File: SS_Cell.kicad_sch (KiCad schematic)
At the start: 12 parts, among them J1 SSC1, U1 ATtiny102-SS, U2 TPS2115

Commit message: 
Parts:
- removed R1, R2, R24: 5K, Resistor_SMD:R_0603_1608Metric, symbol Device:R
- removed TP1: SSC_TPIDATA, TestPoint:TestPoint_Pad_D1.0mm, symbol Connector:TestPoint
- removed TP2: SSC_TPICLK, TestPoint:TestPoint_Pad_D1.0mm, symbol Connector:TestPoint
- removed TP3: SSC_RST, TestPoint:TestPoint_Pad_D1.0mm, symbol Connector:TestPoint
- removed U1: ATtiny102-SS, Package_SO:SOIC-8_3.9x4.9mm_P1.27mm, symbol MCU_Microchip_ATtiny:ATtiny102-SS
- C9: renamed from C1; MPN (none) -> C14663
- J1: now left out of the parts list
- R24: renamed from R25; footprint Resistor_SMD:R_0603_1608Metric -> Resistor_SMD:R_0402_1005Metric; symbol Device:R -> Project:R; MPN (none) -> C477765
- R25: renamed from R26; footprint Resistor_SMD:R_0603_1608Metric -> Resistor_SMD:R_0402_1005Metric; symbol Device:R -> Project:R; MPN (none) -> C25130
- U4: renamed from U2; footprint Package_SO:TSSOP-8_4.4x3mm_P0.65mm -> Library:VSON-8_3.3x3.3mm_P0.65mm_NexFET; JLCPCB Rotation Offset (none) -> -90; MPN (none) -> C140321
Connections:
- net SS_TX: now reaches J1.2 (Pin_2)
- net SS_RX: now reaches J1.3 (Pin_3)
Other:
- moved on the sheet: J1

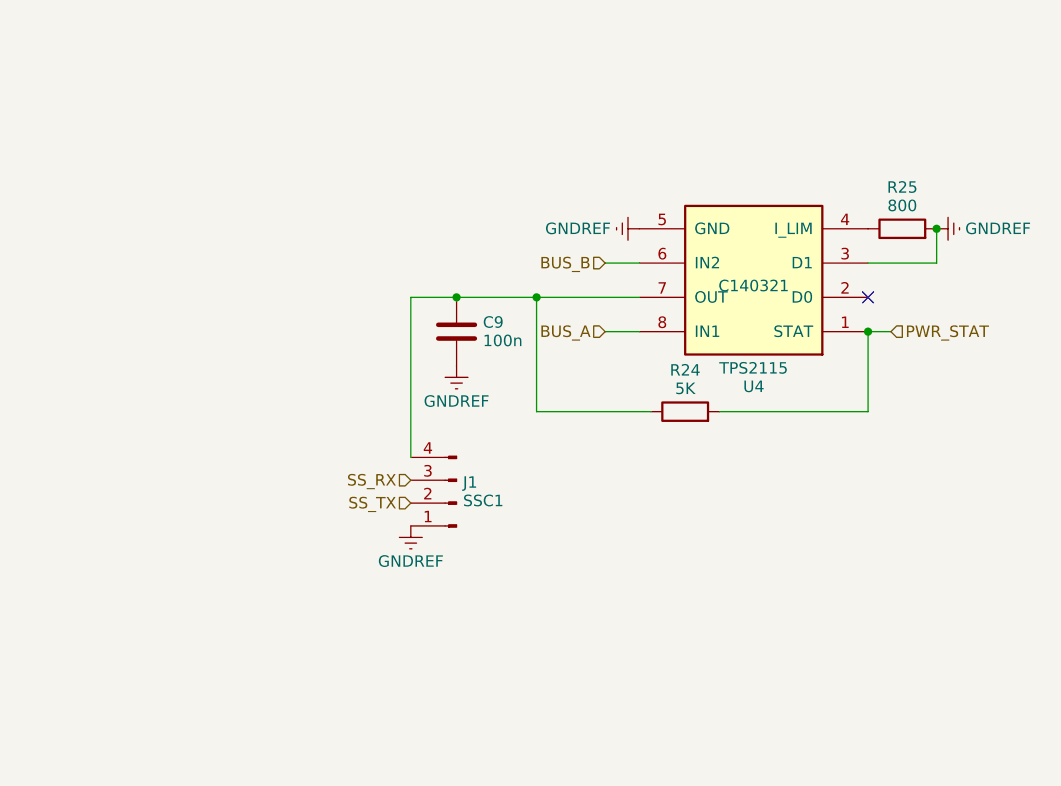
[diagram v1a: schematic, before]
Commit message: Set up STM32 env
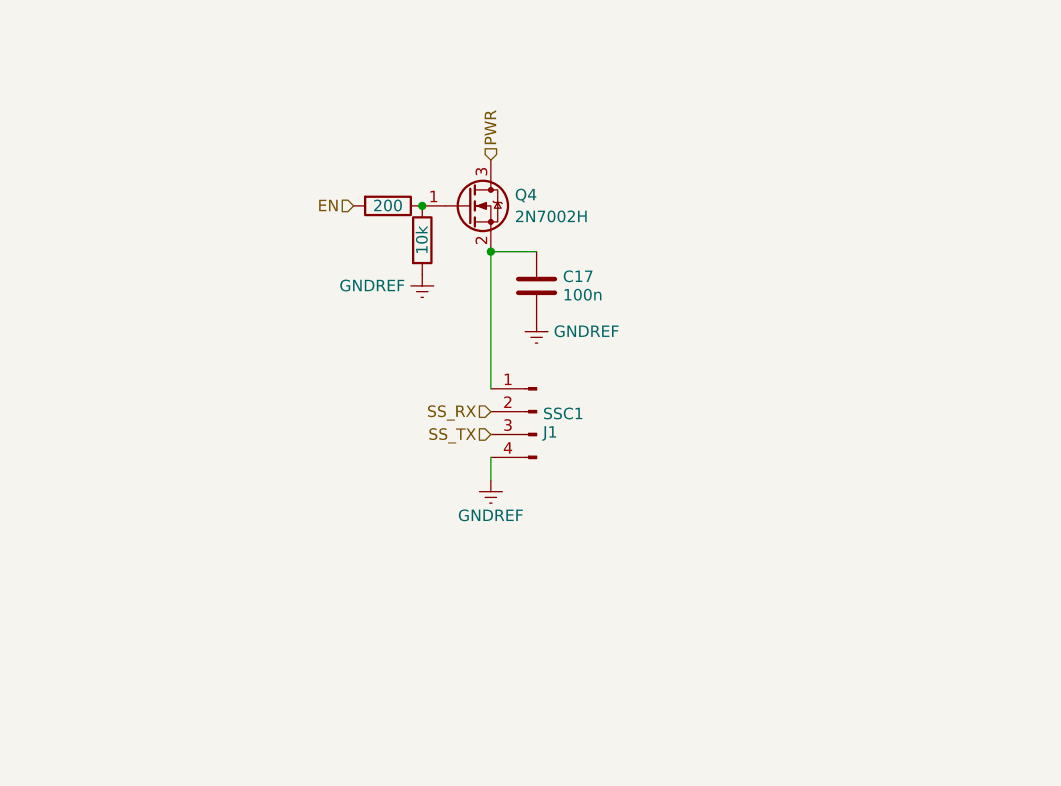
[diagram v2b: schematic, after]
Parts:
- removed C9: 100n, Capacitor_SMD:C_0603_1608Metric, symbol Device:C
- removed J1: SSC1, Connector_PinHeader_1.00mm:PinHeader_1x04_P1.00mm_Vertical, symbol Connector:Conn_01x04_Pin
- removed R24: 5K, Resistor_SMD:R_0402_1005Metric, symbol Project:R
- removed R25: 800, Resistor_SMD:R_0402_1005Metric, symbol Project:R
- removed U4: TPS2115, Library:VSON-8_3.3x3.3mm_P0.65mm_NexFET, symbol Project:TPS2115
- added C17: 100n, Capacitor_SMD:C_0603_1608Metric, symbol Library:C
- added J1: SSC1, Connector_JST:JST_SH_BM04B-SRSS-TB_1x04-1MP_P1.00mm_Vertical, symbol Library:Conn_01x04_Pin
- added Q4: 2N7002H, Package_TO_SOT_SMD:SOT-23, symbol Library:2N7002H
- added R12: 200, Resistor_SMD:R_0402_1005Metric, symbol Library:R
- added R13: 10k, Resistor_SMD:R_0402_1005Metric, symbol Library:R
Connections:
- net GNDREF: now also C17.2, J1.4 (Pin_4), R13.2
- net SS_RX: now also J1.2 (Pin_2)
- net SS_TX: now also J1.3 (Pin_3)
- new net: Q4.1 (G), R12.1, R13.1
- new net: C17.1, J1.1 (Pin_1), Q4.2 (S)
- new net EN: R12.2
- new net PWR: Q4.3 (D)
- no-connect marks 1 -> 0

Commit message: update layout
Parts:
- Q4: value 2N7002H -> DMG1012T; footprint Package_TO_SOT_SMD:SOT-23 -> Package_TO_SOT_SMD:SOT-523; JLC C150714 -> C20512
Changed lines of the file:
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@@
       (effects (font (size 1.27 1.27)) (justify left))
     )
-    (property "Value" "2N7002H" (at 138.557 104.0821 0)
+    (property "Value" "DMG1012T" (at 138.557 104.0821 0)
       (effects (font (size 1.27 1.27)) (justify left))
     )
-    (property "Footprint" "Package_TO_SOT_SMD:SOT-23" (at 138.43 104.775 0)
+    (property "Footprint" "Package_TO_SOT_SMD:SOT-523" (at 138.43 104.775 0)
       (effects (font (size 1.27 1.27) italic) (justify left) hide)
     )
@@
       (effects (font (size 1.27 1.27)) (justify left) hide)
     )
-    (property "JLC" "C150714" (at 133.35 102.87 0)
+    (property "JLC" "C20512" (at 133.35 102.87 0)
       (effects (font (size 1.27 1.27)) hide)
     )

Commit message: Revision 2.1 HW
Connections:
- net GNDREF: now also Q4.2 (S); no longer J1.4 (Pin_4)
- net PWR: now also C17.1, J1.1 (Pin_1); no longer Q4.3 (D)
- new net: J1.4 (Pin_4), Q4.3 (D)
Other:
- moved on the sheet: C17, Q4
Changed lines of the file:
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@@
 (kicad_sch (version 20230121) (generator eeschema)
   (paper "A4")
-  (junction (at 135.89 107.95) (diameter 0) (color 0 0 0 0)
-  )
-  (junction (at 128.27 102.87) (diameter 0) (color 0 0 0 0)
-  )
-  (wire (pts (xy 135.89 123.19) (xy 135.89 107.95))
-    (stroke (width 0) (type default))
-  )
-  (wire (pts (xy 140.97 107.95) (xy 135.89 107.95))
-    (stroke (width 0) (type default))
-  )
-  (wire (pts (xy 135.89 133.35) (xy 135.89 130.81))
+  (junction (at 128.27 135.89) (diameter 0) (color 0 0 0 0)
+  )
+  (wire (pts (xy 124.46 123.19) (xy 135.89 123.19))
     (stroke (width 0) (type default))
   )
@@
     (effects (font (size 1.27 1.27)) (justify right))
   )
-  (hierarchical_label "EN" (shape input) (at 120.65 102.87 180) (fields_autoplaced)
+  (hierarchical_label "EN" (shape input) (at 120.65 135.89 180) (fields_autoplaced)
     (effects (font (size 1.27 1.27)) (justify right))
   )
-  (hierarchical_label "PWR" (shape input) (at 135.89 97.79 90) (fields_autoplaced)
+  (hierarchical_label "PWR" (shape input) (at 124.46 123.19 90) (fields_autoplaced)
     (effects (font (size 1.27 1.27)) (justify left))
   )
-  (symbol (lib_id "Library:R") (at 128.27 106.68 0) (unit 1)
+  (symbol (lib_id "Library:R") (at 128.27 139.7 0) (unit 1)
     (in_bom yes) (on_board yes) (dnp no)
-    (property "Reference" "R13" (at 127 101.6 90)
-      (effects (font (size 1.27 1.27)) hide)
-    )
-    (property "Value" "10k" (at 128.27 106.68 90)
+    (property "Reference" "R13" (at 127 134.62 90)
+      (effects (font (size 1.27 1.27)) hide)
+    )
+    (property "Value" "10k" (at 128.27 139.7 90)
       (effects (font (size 1.27 1.27)))
     )
-    (property "Footprint" "Resistor_SMD:R_0402_1005Metric" (at 126.492 106.68 90)
-      (effects (font (size 1.27 1.27)) hide)
-    )
-    (property "Datasheet" "~" (at 128.27 106.68 0)
-      (effects (font (size 1.27 1.27)) hide)
-    )
-    (property "MPN" "C26083" (at 128.27 106.68 90)
+    (property "Footprint" "Resistor_SMD:R_0402_1005Metric" (at 126.492 139.7 90)
+      (effects (font (size 1.27 1.27)) hide)
+    )
+    (property "Datasheet" "~" (at 128.27 139.7 0)
+      (effects (font (size 1.27 1.27)) hide)
+    )
+    (property "MPN" "C26083" (at 128.27 139.7 90)
       (effects (font (size 1.27 1.27)) hide)
     )
@@
     )
   )
-  (symbol (lib_id "power:GNDREF") (at 128.27 110.49 0) (unit 1)
-    (in_bom yes) (on_board yes) (dnp no) (fields_autoplaced)
-    (property "Reference" "#PWR018" (at 128.27 116.84 0)
-      (effects (font (size 1.27 1.27)) hide)
-    )
-    (property "Value" "GNDREF" (at 126.3651 111.76 0)
-      (effects (font (size 1.27 1.27)) (justify right))
-    )
-    (property "Footprint" "" (at 128.27 110.49 0)
-      (effects (font (size 1.27 1.27)) hide)
-    )
-    (property "Datasheet" "" (at 128.27 110.49 0)
+  (symbol (lib_id "power:GNDREF") (at 128.27 143.51 0) (unit 1)
+    (in_bom yes) (on_board yes) (dnp no) (fields_autoplaced)
+    (property "Reference" "#PWR018" (at 128.27 149.86 0)
+      (effects (font (size 1.27 1.27)) hide)
+    )
+    (property "Value" "GNDREF" (at 126.3651 144.78 0)
+      (effects (font (size 1.27 1.27)) (justify right))
+    )
+    (property "Footprint" "" (at 128.27 143.51 0)
+      (effects (font (size 1.27 1.27)) hide)
+    )
+    (property "Datasheet" "" (at 128.27 143.51 0)
       (effects (font (size 1.27 1.27)) hide)
     )
@@
     )
   )
-  (symbol (lib_id "power:GNDREF") (at 140.97 115.57 0) (unit 1)
-    (in_bom yes) (on_board yes) (dnp no) (fields_autoplaced)
-    (property "Reference" "#PWR01" (at 140.97 121.92 0)
-      (effects (font (size 1.27 1.27)) hide)
-    )
-    (property "Value" "GNDREF" (at 142.875 116.84 0)
-      (effects (font (size 1.27 1.27)) (justify left))
-    )
-    (property "Footprint" "" (at 140.97 115.57 0)
-      (effects (font (size 1.27 1.27)) hide)
-    )
-    (property "Datasheet" "" (at 140.97 115.57 0)
+  (symbol (lib_id "power:GNDREF") (at 124.46 130.81 0) (unit 1)
+    (in_bom yes) (on_board yes) (dnp no) (fields_autoplaced)
+    (property "Reference" "#PWR01" (at 124.46 137.16 0)
+      (effects (font (size 1.27 1.27)) hide)
+    )
+    (property "Value" "GNDREF" (at 122.5551 132.08 0)
+      (effects (font (size 1.27 1.27)) (justify right))
+    )
+    (property "Footprint" "" (at 124.46 130.81 0)
+      (effects (font (size 1.27 1.27)) hide)
+    )
+    (property "Datasheet" "" (at 124.46 130.81 0)
       (effects (font (size 1.27 1.27)) hide)
     )
@@
     )
   )
-  (symbol (lib_id "Library:C") (at 140.97 111.76 0) (unit 1)
-    (in_bom yes) (on_board yes) (dnp no) (fields_autoplaced)
-    (property "Reference" "C17" (at 143.891 110.736 0)
-      (effects (font (size 1.27 1.27)) (justify left))
-    )
-    (property "Value" "100n" (at 143.891 112.784 0)
-      (effects (font (size 1.27 1.27)) (justify left))
-    )
-    (property "Footprint" "Capacitor_SMD:C_0603_1608Metric" (at 141.9352 115.57 0)
-      (effects (font (size 1.27 1.27)) hide)
-    )
-    (property "Datasheet" "~" (at 140.97 111.76 0)
-      (effects (font (size 1.27 1.27)) hide)
-    )
-    (property "MPN" "C14663" (at 140.97 111.76 0)
+  (symbol (lib_id "Library:C") (at 124.46 127 0) (unit 1)
+    (in_bom yes) (on_board yes) (dnp no) (fields_autoplaced)
+    (property "Reference" "C17" (at 121.5391 125.7879 0)
+      (effects (font (size 1.27 1.27)) (justify right))
+    )
+    (property "Value" "100n" (at 121.5391 128.2121 0)
+      (effects (font (size 1.27 1.27)) (justify right))
+    )
+    (property "Footprint" "Capacitor_SMD:C_0603_1608Metric" (at 125.4252 130.81 0)
+      (effects (font (size 1.27 1.27)) hide)
+    )
+    (property "Datasheet" "~" (at 124.46 127 0)
+      (effects (font (size 1.27 1.27)) hide)
+    )
+    (property "MPN" "C14663" (at 124.46 127 0)
       (effects (font (size 1.27 1.27)) hide)
     )
@@
     )
   )
-  (symbol (lib_id "Library:R") (at 124.46 102.87 270) (unit 1)
+  (symbol (lib_id "Library:R") (at 124.46 135.89 270) (unit 1)
     (in_bom yes) (on_board yes) (dnp no)
-    (property "Reference" "R12" (at 129.54 101.6 90)
-      (effects (font (size 1.27 1.27)) hide)
-    )
-    (property "Value" "200" (at 124.46 102.87 90)
+    (property "Reference" "R12" (at 129.54 134.62 90)
+      (effects (font (size 1.27 1.27)) hide)
+    )
+    (property "Value" "200" (at 124.46 135.89 90)
       (effects (font (size 1.27 1.27)))
     )
-    (property "Footprint" "Resistor_SMD:R_0402_1005Metric" (at 124.46 101.092 90)
-      (effects (font (size 1.27 1.27)) hide)
-    )
-    (property "Datasheet" "~" (at 124.46 102.87 0)
-      (effects (font (size 1.27 1.27)) hide)
-    )
-    (property "MPN" "C25087" (at 124.46 102.87 90)
+    (property "Footprint" "Resistor_SMD:R_0402_1005Metric" (at 124.46 134.112 90)
+      (effects (font (size 1.27 1.27)) hide)
+    )
+    (property "Datasheet" "~" (at 124.46 135.89 0)
+      (effects (font (size 1.27 1.27)) hide)
+    )
+    (property "MPN" "C25087" (at 124.46 135.89 90)
       (effects (font (size 1.27 1.27)) hide)
     )
@@
     )
   )
-  (symbol (lib_id "power:GNDREF") (at 135.89 133.35 0) (unit 1)
-    (in_bom yes) (on_board yes) (dnp no) (fields_autoplaced)
-    (property "Reference" "#PWR019" (at 135.89 139.7 0)
-      (effects (font (size 1.27 1.27)) hide)
-    )
-    (property "Value" "GNDREF" (at 135.89 137.295 0)
+  (symbol (lib_id "power:GNDREF") (at 135.89 140.97 0) (unit 1)
+    (in_bom yes) (on_board yes) (dnp no) (fields_autoplaced)
+    (property "Reference" "#PWR019" (at 135.89 147.32 0)
+      (effects (font (size 1.27 1.27)) hide)
+    )
+    (property "Value" "GNDREF" (at 135.89 144.915 0)
       (effects (font (size 1.27 1.27)))
     )
-    (property "Footprint" "" (at 135.89 133.35 0)
-      (effects (font (size 1.27 1.27)) hide)
-    )
-    (property "Datasheet" "" (at 135.89 133.35 0)
+    (property "Footprint" "" (at 135.89 140.97 0)
+      (effects (font (size 1.27 1.27)) hide)
+    )
+    (property "Datasheet" "" (at 135.89 140.97 0)
       (effects (font (size 1.27 1.27)) hide)
     )
@@
     )
   )
-  (symbol (lib_id "Library:2N7002H") (at 133.35 102.87 0) (unit 1)
-    (in_bom yes) (on_board yes) (dnp no) (fields_autoplaced)
-    (property "Reference" "Q4" (at 138.557 101.6579 0)
+  (symbol (lib_id "Library:2N7002H") (at 133.35 135.89 0) (unit 1)
+    (in_bom yes) (on_board yes) (dnp no) (fields_autoplaced)
+    (property "Reference" "Q4" (at 138.557 134.6779 0)
       (effects (font (size 1.27 1.27)) (justify left))
     )
-    (property "Value" "DMG1012T" (at 138.557 104.0821 0)
+    (property "Value" "DMG1012T" (at 138.557 137.1021 0)
       (effects (font (size 1.27 1.27)) (justify left))
     )
-    (property "Footprint" "Package_TO_SOT_SMD:SOT-523" (at 138.43 104.775 0)
+    (property "Footprint" "Package_TO_SOT_SMD:SOT-523" (at 138.43 137.795 0)
       (effects (font (size 1.27 1.27) italic) (justify left) hide)
     )
-    (property "Datasheet" "http://www.diodes.com/assets/Datasheets/2N7002H.pdf" (at 133.35 102.87 0)
+    (property "Datasheet" "http://www.diodes.com/assets/Datasheets/2N7002H.pdf" (at 133.35 135.89 0)
       (effects (font (size 1.27 1.27)) (justify left) hide)
     )
-    (property "JLC" "C20512" (at 133.35 102.87 0)
-      (effects (font (size 1.27 1.27)) hide)
-    )
+    (property "JLC" "C20512" (at 133.35 135.89 0)
+      (effects (font (size 1.27 1.27)) hide)
+    )
